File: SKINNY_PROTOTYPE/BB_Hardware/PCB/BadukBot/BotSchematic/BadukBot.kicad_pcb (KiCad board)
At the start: 4 copper layers, 22.4 x 92.3 mm, 72 parts, among them J1 MOLEX_78171-0002, J10 A3-16DA-2SV(71), J11 62401621722, J12 803-87-010-10-001101, J13 67997-410HLF, J2 MOLEX_78171-0003, Q1 MMBT3904LT1G, Q2 MMBT3904LT1G, Q3 MMBT3904LT1G, Q4 MMBT3904LT1G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

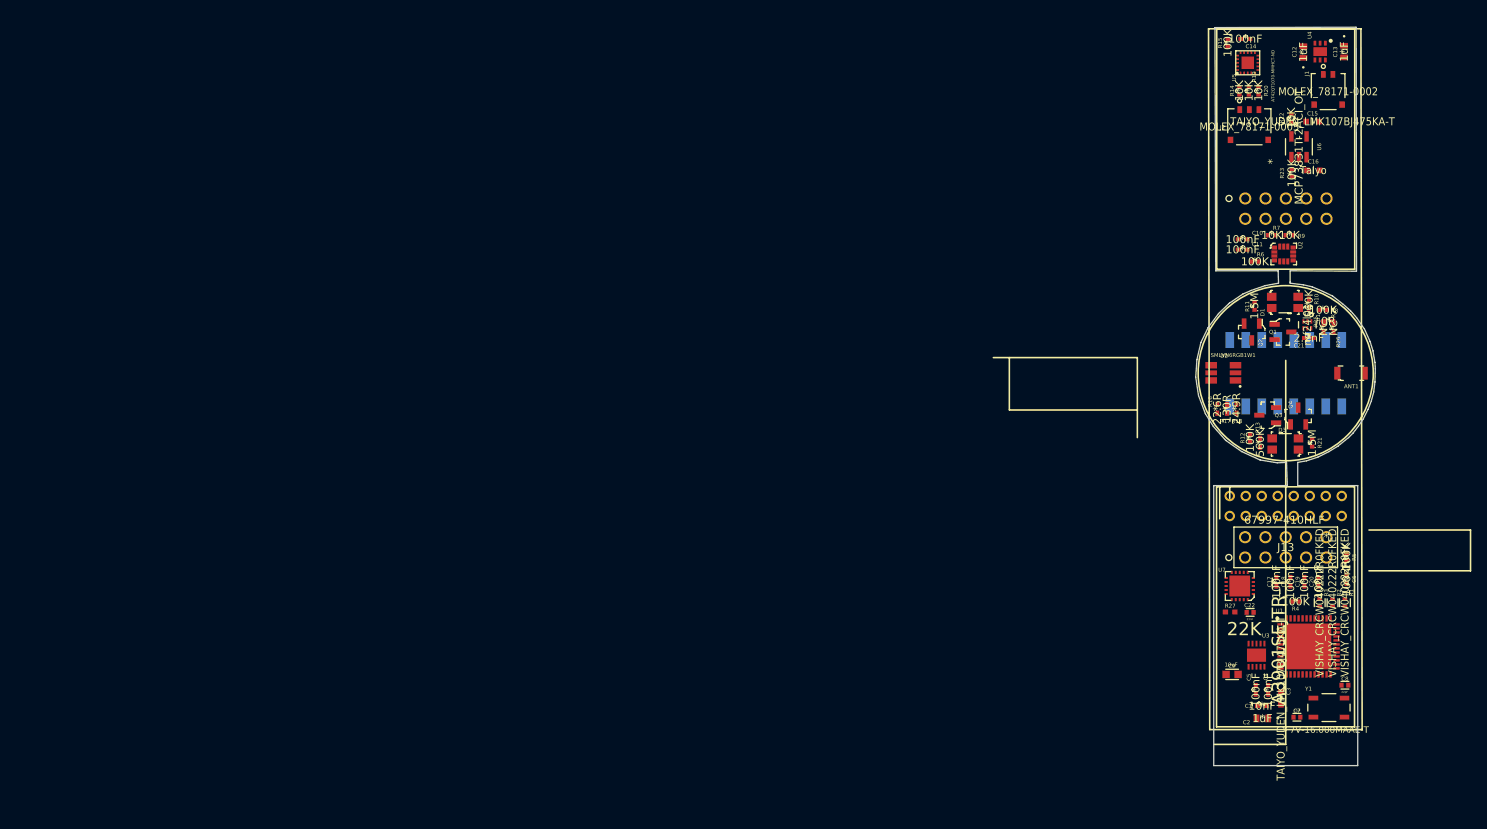
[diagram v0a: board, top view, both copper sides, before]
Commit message: Images of original board's layers; images of current work setup; updated schematics and BOM to change connectors; major boards revisions
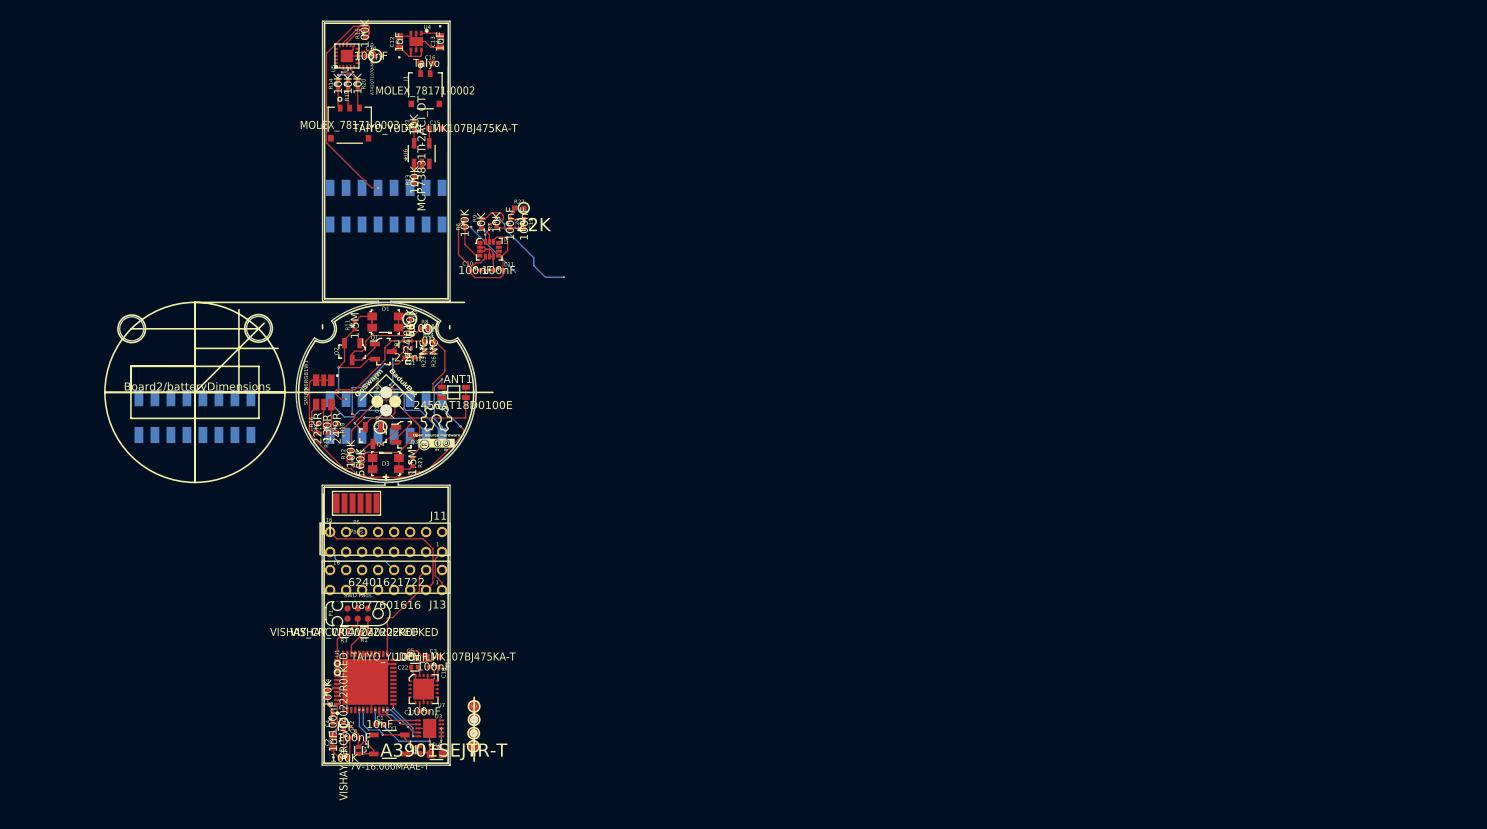
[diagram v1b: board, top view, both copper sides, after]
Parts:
- added G1: LOGO, Silk:BadukBot-GoSwarm, F.Cu at (110.0, 115.2)
- added G2: LOGO, Silk:OpenHardwareLogo, F.Cu at (116.2, 119.3)
- added J12: A3-16DA-2SV(71), A13:A13, B.Cu at (86.0, 117.3)
- added M1: Pos-1a, gsg-modules:TESTPOINT-50MIL, F.Cu at (120.8, 159.2)
- added M2: Neg-1a, gsg-modules:TESTPOINT-50MIL, F.Cu at (120.9, 157.6)
- added M3: Pos-2a, gsg-modules:TESTPOINT-50MIL, F.Cu at (121.0, 154.2)
- added M4: Neg-2a, gsg-modules:TESTPOINT-50MIL, F.Cu at (121.0, 155.8)
- added P1: SWD Pads, library:SWD_6pin, F.Cu at (106.4, 142.6)
- added P4: Conn_01x02_Female, Connector_DIN:Conn_01x02_Female, F.Cu at (110.0, 116.0)
- added P5: Pads, library:ExternalPort, F.Cu at (106.2, 128.8)
- ANT1: value Antenna -> 2450AT18D0100E; footprint digikey-footprints:Antenna_1.6x3.2mm_2450AT18A100E -> 2450AT18D0100E:DFN320X160X120-4RN
- J10: footprint 16pos_2mm_SMD:A13 -> A13:A13
- J11: moved to F.Cu
- J12: value 803-87-010-10-001101 -> A3-16DA-2SV(71); footprint 2x5conn:2x5 -> A13:A13
- J13: value 67997-410HLF -> 0877601616; footprint 2x5conn:2x5 -> 16pos_2mm_RA:0877601616
- U5: footprint AT42QT1070-MMHCT-ND:VQFN_20PAD -> vq:VQFN_20PAD
- moved R5 127.8 mm to (104.7, 160.7), turned to 180 degrees
- moved C6 125.6 mm to (106.0, 158.1), turned to 0 degrees
- moved R2 124.6 mm to (104.7, 156.7)
- moved R1 122.6 mm to (107.2, 144.9), turned to 180 degrees
- moved R3 122.0 mm to (104.7, 144.9), turned to 180 degrees
- moved R4 121.5 mm to (102.7, 152.6), turned to 270 degrees
- moved U1 118.0 mm to (107.3, 151.2), turned to 90 degrees
- moved J13 117.7 mm to (110.0, 138.4)
- moved J12 117.6 mm to (110.0, 91.0)
- moved Y1 117.5 mm to (110.3, 158.9)
- moved C7 117.4 mm to (106.5, 159.7), turned to 90 degrees
- moved C4 117.0 mm to (103.3, 155.7)
- moved C2 116.2 mm to (103.3, 158.7), turned to 90 degrees
- moved C8 115.9 mm to (114.2, 159.6), turned to 270 degrees
- moved Q4 115.7 mm to (108.3, 120.3), turned to 270 degrees
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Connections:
- net 10a_SDA renamed Net-(J10-Pad10)
- net 11a_SCL renamed Net-(J10-Pad11)
- net 15a_GND2 renamed Net-(J10-Pad16)
- net 8a_IO1 renamed Net-(J10-Pad8)
- net 9a_IO2 renamed Net-(J10-Pad9)
- ANT1 pad 2: Net-(ANT1-Pad2) -> 2a_GND
- C1 pad 2: 15b_GND2 -> 2b_GND
- C10 pad 2: 23a_GND -> 21a_3.3v
- C11 pad 2: 23a_GND -> 21a_3.3v
- C12 pad 2: 23a_GND -> 21a_3.3v
- C13 pad 2: 23a_GND -> 21a_3.3v
- C14 pad 2: 23a_GND -> 21a_3.3v
- C15 pad 2: 23a_GND -> 21a_3.3v
- C16 pad 2: 23a_GND -> 21a_3.3v
- C17 pad 1: 15b_GND2 -> 2b_GND
- C18 pad 1: 15b_GND2 -> 2b_GND
- C19 pad 1: 15b_GND2 -> 2b_GND
- C2 pad 2: 15b_GND2 -> 2b_GND
- C20 pad 1: 15b_GND2 -> 2b_GND
- C22 pad 2: 15b_GND2 -> 2b_GND
- C3 pad 2: 15b_GND2 -> 2b_GND
- C4 pad 2: 15b_GND2 -> 2b_GND
- C5 pad 2: 15b_GND2 -> 2b_GND
- C6 pad 2: 15b_GND2 -> 2b_GND
- C7 pad 2: 15b_GND2 -> 2b_GND
- C8 pad 2: 15b_GND2 -> 2b_GND
- C9 pad 2: 15b_GND2 -> 2b_GND
- J1 pad 2: 23a_GND -> 21a_3.3v
- J11 pad 10: 10b_SDA -> Net-(J11-Pad10)
- J11 pad 11: 11b_SCL -> Net-(J11-Pad11)
- J11 pad 16: 15b_GND2 -> 2b_GND
- J11 pad 2: 15b_GND2 -> Net-(J11-Pad2)
- J11 pad 8: 8b_IO1 -> Net-(J11-Pad8)
- J11 pad 9: 9b_IO2 -> Net-(J11-Pad9)
- J12 pad 10: 21a_3.3v -> Net-(J12-Pad10)
- J12 pad 2: 22a_VBAT -> 21a_3.3v
- J12 pad 3: 23a_GND -> 22a_VBAT
- J13 pad 10: 1b_3.3v -> Net-(J13-Pad10)
- J13 pad 3: 15b_GND2 -> 2b_GND
- R16 pad 1: 6a_RGBLED2 -> Net-(R16-Pad1)
- R17 pad 1: 5a_RGBLED1 -> Net-(R17-Pad1)
- R18 pad 1: 7a_RGBLED3 -> Net-(R18-Pad1)
- R22 pad 1: 23a_GND -> 21a_3.3v
- R27 pad 1: 15b_GND2 -> 2b_GND
- R4 pad 2: 15b_GND2 -> 2b_GND
- U1 pad 23: 15b_GND2 -> 2b_GND
- U1 pad 47: 15b_GND2 -> 2b_GND
- U1 pad 49: 15b_GND2 -> 2b_GND
- U1 pad 8: 15b_GND2 -> 2b_GND
- U2 pad 1: 23a_GND -> 21a_3.3v
- U2 pad 2: 23a_GND -> 21a_3.3v
- U2 pad 3: 23a_GND -> 21a_3.3v
- U2 pad 6: 23a_GND -> 21a_3.3v
- U2 pad 7: 23a_GND -> 21a_3.3v
- U2 pad 9: Net-(U2-Pad9) -> 21a_3.3v
- U3 pad 11: Net-(U3-Pad11) -> 2b_GND
- U3 pad 3: Net-(U3-Pad3) -> 2b_GND
- U4 pad 2: Net-(U4-Pad2) -> 21a_3.3v
- U4 pad 3: 23a_GND -> 21a_3.3v
- U4 pad 5: Net-(U4-Pad5) -> 21a_3.3v
- U4 pad 7: Net-(U4-Pad7) -> 21a_3.3v
- U5 pad 11: 23a_GND -> 21a_3.3v
- U5 pad 13: 23a_GND -> 21a_3.3v
- U5 pad 8: 23a_GND -> 21a_3.3v
- U5 pad 9: 23a_GND -> 21a_3.3v
- U6 pad 2: 23a_GND -> 21a_3.3v
- U7 pad 14: 15b_GND2 -> 2b_GND
- U7 pad 17: 15b_GND2 -> 2b_GND
- U7 pad 20: 15b_GND2 -> 2b_GND
- U7 pad 21: 15b_GND2 -> 2b_GND
- U7 pad 8: 15b_GND2 -> 2b_GND
- Y1 pad 2: Net-(Y1-Pad2) -> 2b_GND
- Y1 pad 4: Net-(Y1-Pad4) -> 2b_GND
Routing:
- net 2b_GND: track 0.00 -> 73.3 mm, vias 0 -> 2
- net 15a_GND2: track 0.00 -> 70.6 mm, vias 0 -> 4
- net 21a_3.3v: track 0.00 -> 53.6 mm
- net 1a_3.3v: track 0.00 -> 43.5 mm, vias 0 -> 3
- net ~29a_TOUCH_CHG~: track 0.00 -> 34.4 mm, vias 0 -> 1
- net 1b_3.3v: track 0.00 -> 31.8 mm, vias 0 -> 4
- net 4a_PHOTODIODE2: track 0.00 -> 25.8 mm, vias 0 -> 1
- net 14a_VDD_PA: track 0.00 -> 16.4 mm, vias 0 -> 3
- net 25a_SDA: track 0.00 -> 16.0 mm, vias 0 -> 4
- net 12a_ANT1: track 0.00 -> 15.5 mm, vias 0 -> 3
- net Net-(Q1-Pad1): track 0.00 -> 14.1 mm
- net 13a_ANT2: track 0.00 -> 13.9 mm, vias 0 -> 1
- net 24a_IMU_INT: track 0.00 -> 13.4 mm, vias 0 -> 1
- net 24b_IMU_INT: track 0.00 -> 12.9 mm
- net MCU_X2_16MHZ: track 0.00 -> 10.6 mm, vias 0 -> 2
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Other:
- board size 22.4 x 92.3 mm -> 44.5 x 93 mm
- board text added: "Board1/3HeaderDimensions"
- board text added: "Board1_topDownFootprint"
- board text added: "Board2/batteryDimensions"
- board text added: "Board3_topDownFootprint"

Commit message: Routed PCBs pending optimization
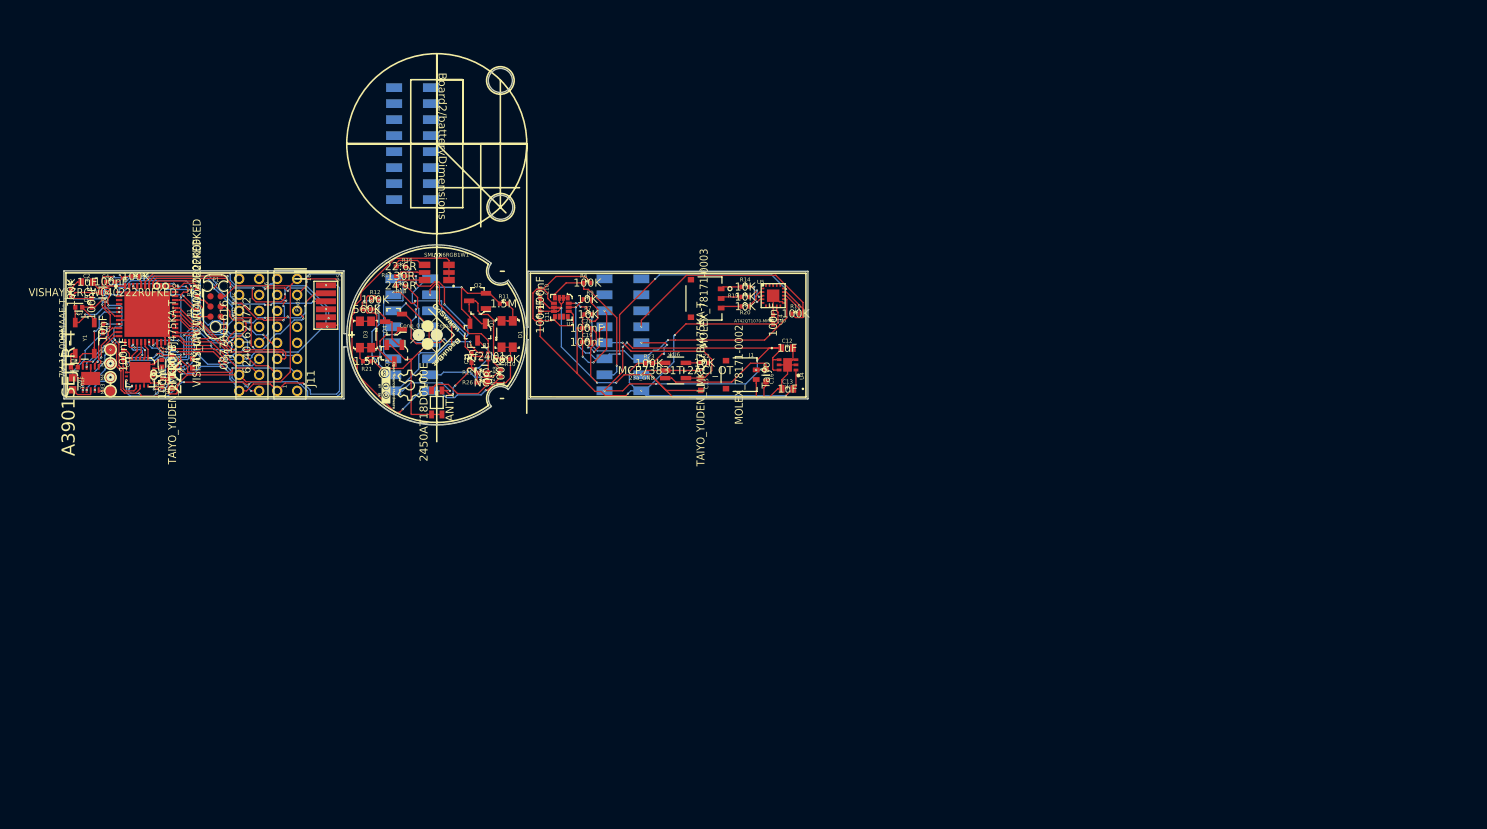
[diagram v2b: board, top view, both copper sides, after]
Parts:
- moved R5 67.4 mm to (70.6, 102.5), turned to 90 degrees
- moved M1 67.2 mm to (75.5, 109.6), turned to 180 degrees
- moved C7 65.5 mm to (71.5, 104.3), turned to 0 degrees
- moved C2 65.2 mm to (72.6, 101.2), turned to 0 degrees
- moved C9 64.9 mm to (70.8, 113.9), turned to 90 degrees
- moved M2 64.8 mm to (75.5, 111.3), turned to 180 degrees
- moved C8 64.4 mm to (71.0, 111.8), turned to 180 degrees
- moved R15 64.2 mm to (161.1, 105.1), turned to 0 degrees
- moved C6 63.5 mm to (73.1, 103.8), turned to 270 degrees
- moved Y1 63.5 mm to (72.3, 108.2), turned to 270 degrees
- moved M4 62.4 mm to (75.5, 113.1), turned to 180 degrees
- moved R2 62.0 mm to (74.5, 102.5), turned to 180 degrees
- moved C12 61.8 mm to (160.1, 109.4), turned to 0 degrees
- moved U4 61.6 mm to (160.1, 111.5), turned to 180 degrees
- moved C13 61.4 mm to (160.1, 114.5), turned to 180 degrees
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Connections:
- C10 pad 2: 21a_3.3v -> 23a_Ground
- C11 pad 2: 21a_3.3v -> 23a_Ground
- C12 pad 2: 21a_3.3v -> 23a_Ground
- C13 pad 2: 21a_3.3v -> 23a_Ground
- C14 pad 2: 21a_3.3v -> 23a_Ground
- C15 pad 2: 21a_3.3v -> 23a_Ground
- C16 pad 2: 21a_3.3v -> 23a_Ground
- C19 pad 1: 2b_GND -> 23a_Ground
- C19 pad 2: 1b_3.3v -> 21a_3.3v
- C20 pad 1: 2b_GND -> 23a_Ground
- C20 pad 2: 1b_3.3v -> 21a_3.3v
- J1 pad 2: 21a_3.3v -> 23a_Ground
- J12 pad 10: Net-(J12-Pad10) -> 23a_Ground
- J12 pad 12: Net-(J12-Pad12) -> 21a_3.3v
- J12 pad 2: 21a_3.3v -> 22a_VBAT
- J12 pad 3: 22a_VBAT -> 23a_Ground
- R16 pad 1: Net-(R16-Pad1) -> 6a_RGBLED2
- R17 pad 1: Net-(R17-Pad1) -> 5a_RGBLED1
- R18 pad 1: Net-(R18-Pad1) -> 7a_RGBLED3
- R22 pad 1: 21a_3.3v -> 23a_Ground
- U1 pad 7: NSRT -> NRST
- U2 pad 1: 21a_3.3v -> 23a_Ground
- U2 pad 2: 21a_3.3v -> 23a_Ground
- U2 pad 3: 21a_3.3v -> 23a_Ground
- U2 pad 6: 21a_3.3v -> 23a_Ground
- U2 pad 7: 21a_3.3v -> 23a_Ground
- U2 pad 9: 21a_3.3v -> Net-(U2-Pad9)
- U4 pad 2: 21a_3.3v -> 23a_Ground
- U4 pad 3: 21a_3.3v -> 23a_Ground
- U4 pad 5: 21a_3.3v -> 23a_Ground
- U4 pad 7: 21a_3.3v -> 23a_Ground
- U5 pad 11: 21a_3.3v -> 23a_Ground
- U5 pad 13: 21a_3.3v -> 23a_Ground
- U5 pad 44: 21a_3.3v -> 23a_Ground
- U5 pad 8: 21a_3.3v -> 23a_Ground
- U5 pad 9: 21a_3.3v -> 23a_Ground
- U6 pad 2: 21a_3.3v -> 23a_Ground
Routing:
- net 23a_Ground: track 0.00 -> 98.5 mm, vias 0 -> 8
- net 21a_3.3v: track 53.6 -> 121.6 mm, vias 0 -> 8
- net 22a_VBAT: track 6.42 -> 73.2 mm, vias 0 -> 7
- net 12b_ANT1: track 0.00 -> 56.2 mm, vias 0 -> 8
- net 14b_VDD_PA: track 0.00 -> 52.0 mm, vias 0 -> 6
- net 10b_SDA: track 0.00 -> 52.0 mm, vias 0 -> 7
- net 13b_ANT2: track 0.00 -> 48.5 mm, vias 0 -> 7
- net 11b_SCL: track 0.00 -> 44.4 mm, vias 0 -> 7
- net 1b_3.3v: track 31.8 -> 74.4 mm, vias 4 -> 11
- net 26a_SCL: track 2.28 -> 42.3 mm, vias 0 -> 4
- net 2b_GND: track 73.3 -> 113.3 mm, vias 2 -> 9
- net Net-(P1-Pad3): track 0.00 -> 36.1 mm, vias 0 -> 10
- net 22b_VBAT: track 0.00 -> 30.9 mm, vias 0 -> 6
- net 8b_IO1: track 0.00 -> 30.8 mm, vias 0 -> 4
- net 3b_PHOTODIODE1: track 0.00 -> 26.8 mm, vias 0 -> 6
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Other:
- board size 44.5 x 93 mm -> 93 x 44.5 mm
- board text added: "23a_GND"
- board text added: "j13-10"
- board text added: "j13-12"
